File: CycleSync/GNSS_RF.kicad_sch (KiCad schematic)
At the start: 0 parts

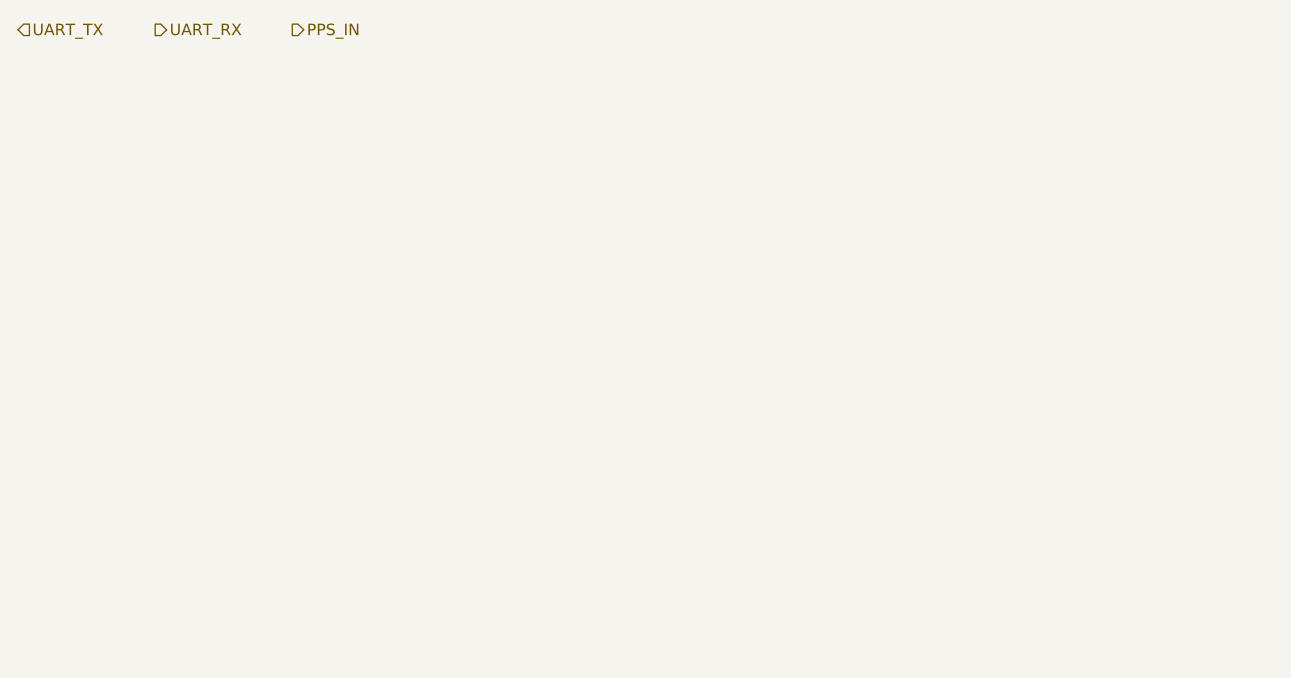
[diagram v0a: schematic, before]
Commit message: M1.3: add LC76G symbol (SnapEDA-sourced), correct pin 5 AP_REQ->RESERVED per Table 6 v1.3
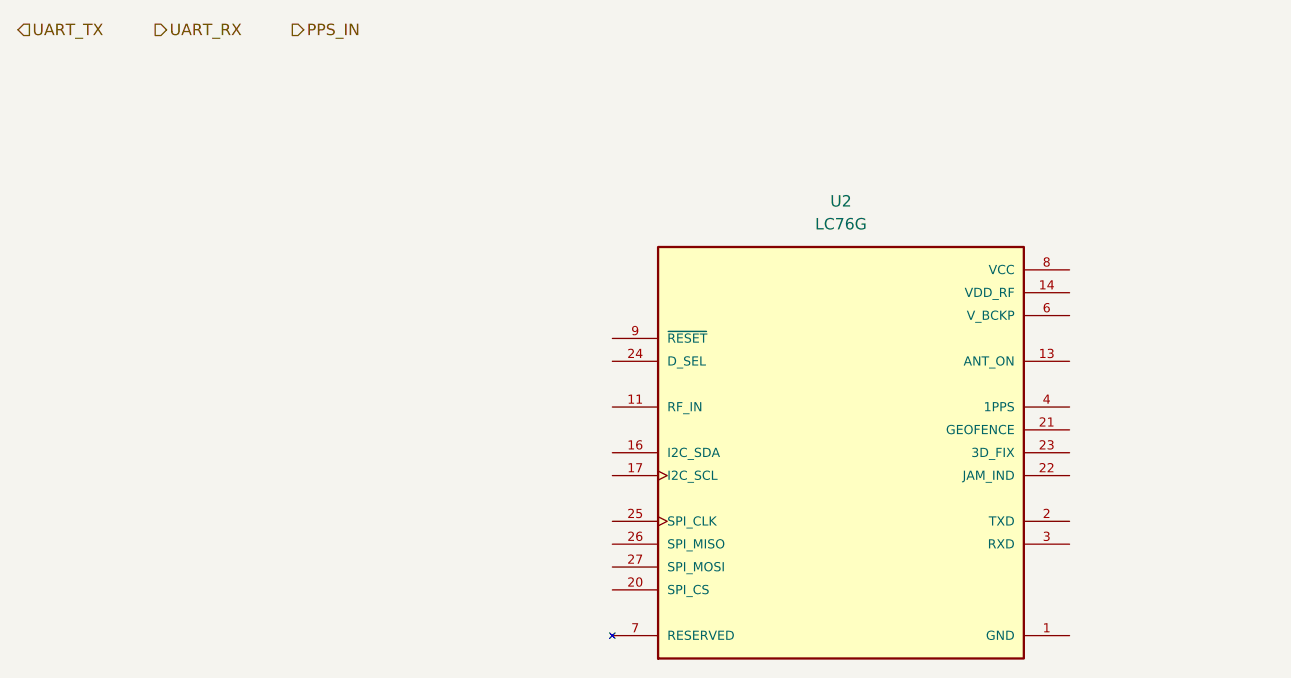
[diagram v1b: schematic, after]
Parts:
- added U2: LC76G, LC76G:XCVR_LC76G, symbol LC76G:LC76G
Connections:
- new net: U2.15 (RESERVED), U2.18 (RESERVED), U2.19 (RESERVED), U2.5 (RESERVED), U2.7 (RESERVED)
- new net GND: U2.1 (GND), U2.10 (GND), U2.12 (GND), U2.28 (GND)

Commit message: M1.3: wire UART_TX/UART_RX/PPS_IN on GNSS_RF sheet (D-009 net names)
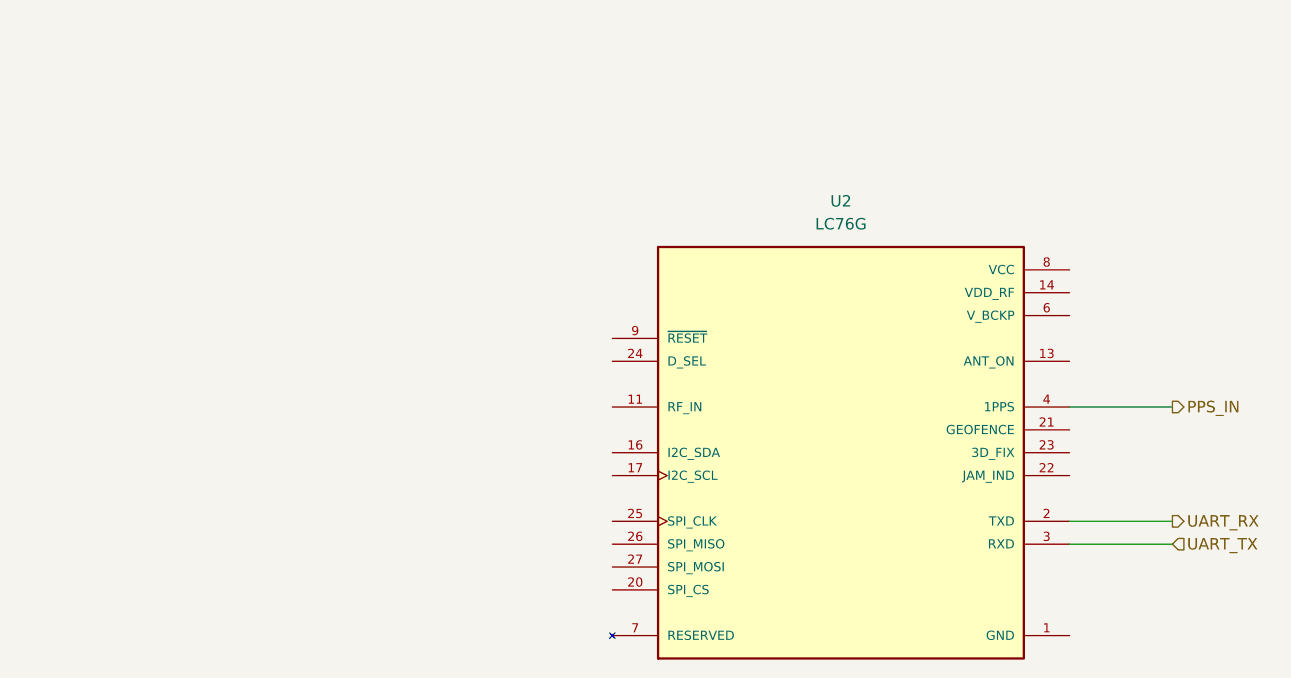
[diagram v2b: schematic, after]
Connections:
- net PPS_IN: now also U2.4 (1PPS)
- net UART_RX: now also U2.2 (TXD)
- net UART_TX: now also U2.3 (RXD)
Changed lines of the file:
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@@
 	(generator_version "10.0")
 	(paper "A4")
+	(wire
+		(pts
+			(xy 152.4 99.06) (xy 163.83 99.06)
+		)
+		(stroke
+			(width 0)
+			(type default)
+		)
+	)
+	(wire
+		(pts
+			(xy 152.4 83.82) (xy 163.83 83.82)
+		)
+		(stroke
+			(width 0)
+			(type default)
+		)
+	)
+	(wire
+		(pts
+			(xy 152.4 96.52) (xy 163.83 96.52)
+		)
+		(stroke
+			(width 0)
+			(type default)
+		)
+	)
 	(hierarchical_label "UART_RX"
 		(shape output)
-		(at 50.8 41.91 0)
+		(at 163.83 96.52 0)
 		(effects
 			(font
@@
 	(hierarchical_label "PPS_IN"
 		(shape output)
-		(at 66.04 41.91 0)
+		(at 163.83 83.82 0)
 		(effects
 			(font
@@
 	(hierarchical_label "UART_TX"
 		(shape input)
-		(at 35.56 41.91 0)
+		(at 163.83 99.06 0)
 		(effects
 			(font
